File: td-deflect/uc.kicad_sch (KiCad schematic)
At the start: 18 parts, among them J4 Conn_ARM_JTAG_SWD_10, J6 Conn_01x06_Male, U12 LM1117-5.0, U2 STM32G474xx, U3 INA193, U4 TPS70933, X1 SG-8002CA

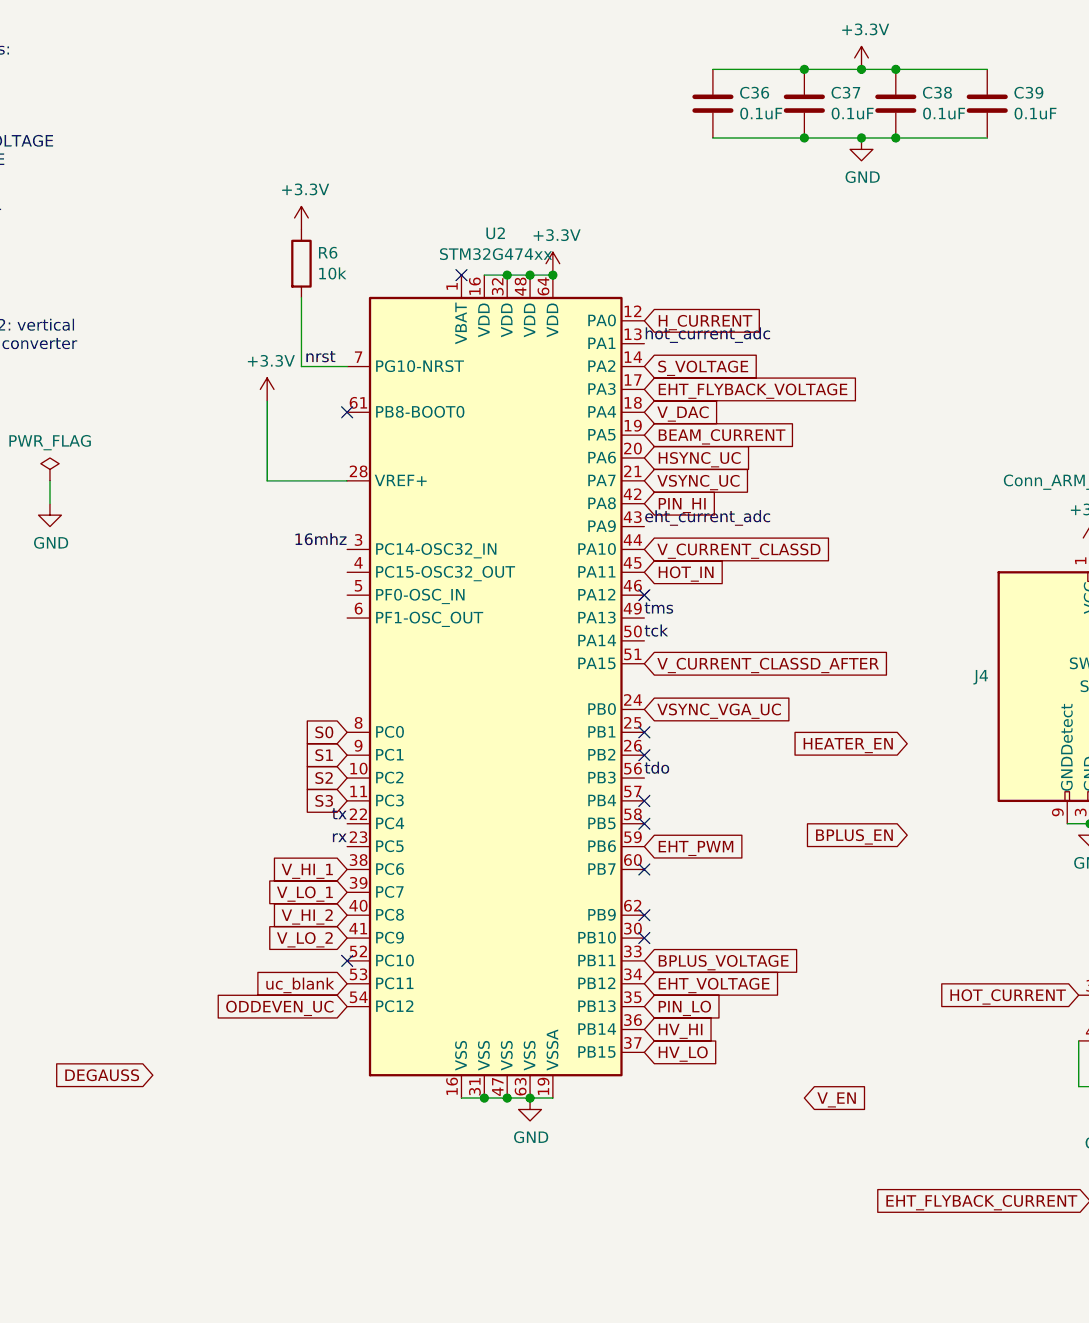
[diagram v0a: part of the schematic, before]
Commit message: switch to kicad official uc symbol
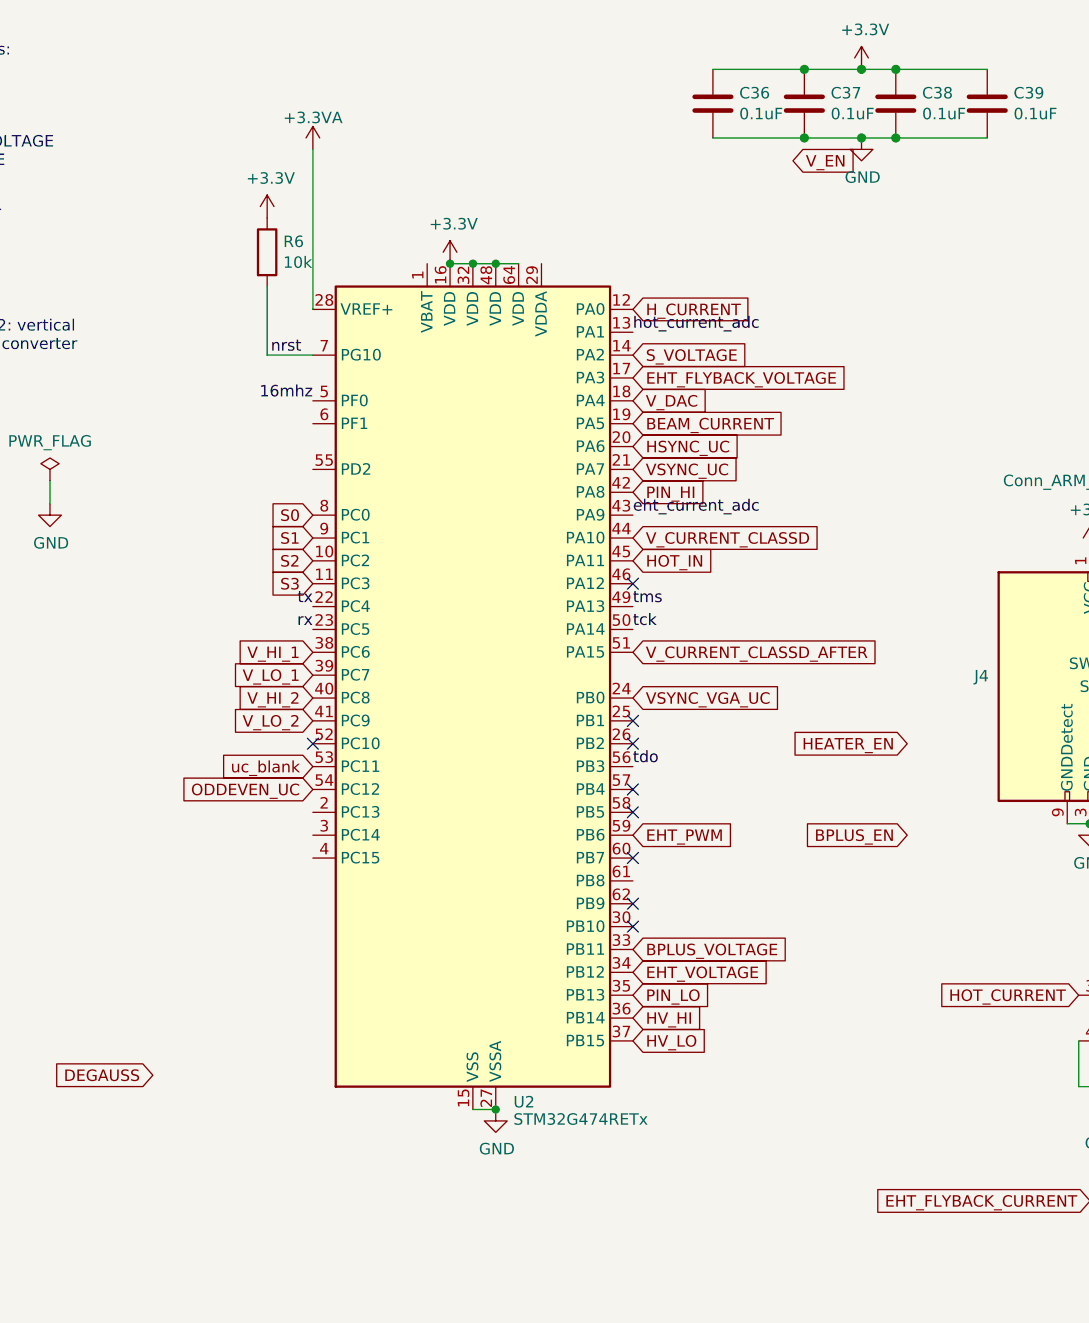
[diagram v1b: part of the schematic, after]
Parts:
- removed U2: STM32G474xx, Package_QFP:LQFP-64_10x10mm_P0.5mm, symbol td-crt:STM32G474xx
- added U2: STM32G474RETx, Package_QFP:LQFP-64_10x10mm_P0.5mm, symbol MCU_ST_STM32G4:STM32G474RETx
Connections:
- net +3V3: now also U2.16 (VDD), U2.32 (VDD), U2.48 (VDD), U2.64 (VDD)
- net 16mhz: now also U2.5 (PF0)
- net BEAM_CURRENT: now also U2.19 (PA5)
- net BPLUS_VOLTAGE: now also U2.33 (PB11)
- net EHT_FLYBACK_VOLTAGE: now also U2.17 (PA3)
- net EHT_PWM: now also U2.59 (PB6)
- net EHT_VOLTAGE: now also U2.34 (PB12)
- net GND: now also U2.15 (VSS), U2.27 (VSSA), U2.31 (VSS), U2.47 (VSS), U2.63 (VSS)
- net HOT_IN: now also U2.45 (PA11)
- net HSYNC_UC: now also U2.20 (PA6)
- net HV_HI: now also U2.36 (PB14)
- net HV_LO: now also U2.37 (PB15)
- net H_CURRENT: now also U2.12 (PA0)
- net ODDEVEN_UC: now also U2.54 (PC12)
- net PIN_HI: now also U2.42 (PA8)
- net PIN_LO: now also U2.35 (PB13)
- net S0: now also U2.8 (PC0)
- net S1: now also U2.9 (PC1)
- net S2: now also U2.10 (PC2)
- net S3: now also U2.11 (PC3)
- net S_VOLTAGE: now also U2.14 (PA2)
- net VSYNC_UC: now also U2.21 (PA7)
- net VSYNC_VGA_UC: now also U2.24 (PB0)
- net V_CURRENT_CLASSD: now also U2.44 (PA10)
- net V_CURRENT_CLASSD_AFTER: now also U2.51 (PA15)
- net V_DAC: now also U2.18 (PA4)
- net V_HI_1: now also U2.38 (PC6)
- net V_HI_2: now also U2.40 (PC8)
- net V_LO_1: now also U2.39 (PC7)
- net V_LO_2: now also U2.41 (PC9)
- net eht_current_adc: now also U2.43 (PA9)
- net hot_current_adc: now also U2.13 (PA1)
- net nrst: now also U2.7 (PG10)
- net rx: now also U2.23 (PC5)
- net tck: now also U2.50 (PA14)
- net tdo: now also U2.56 (PB3)
- net tms: now also U2.49 (PA13)
- net tx: now also U2.22 (PC4)
- net uc_blank: now also U2.53 (PC11)
- new net +3.3VA: U2.28 (VREF+)
- no-connect marks 15 -> 13

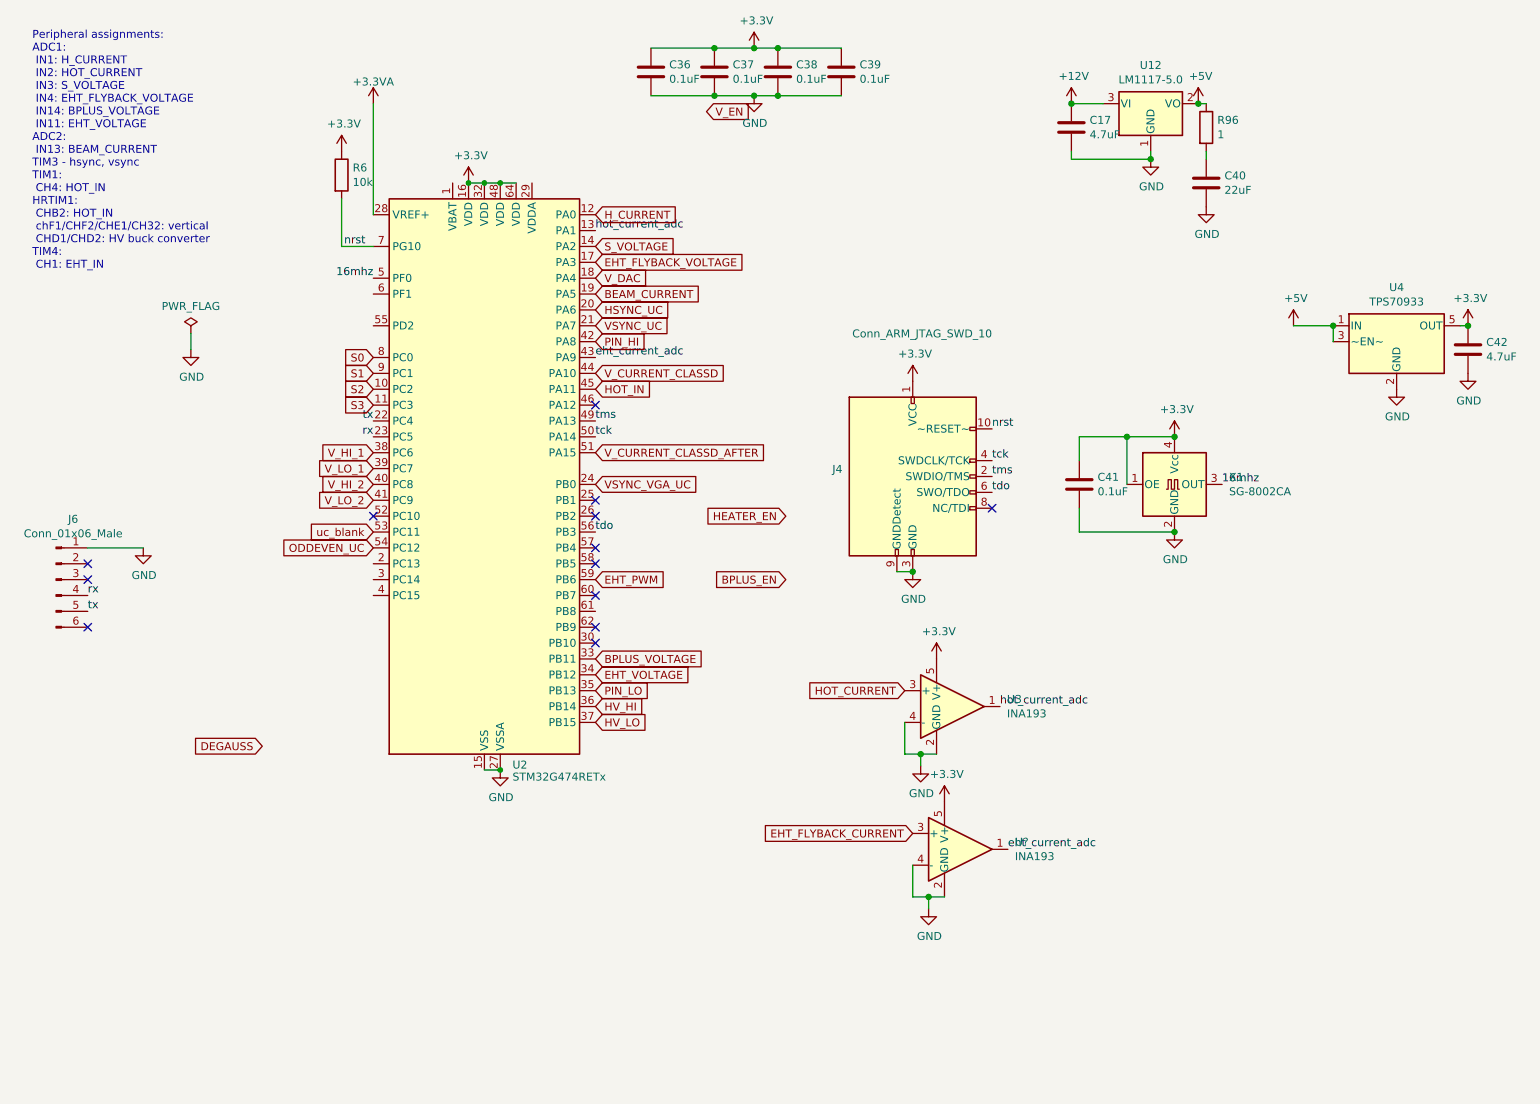
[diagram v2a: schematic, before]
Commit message: add separate analog power supply
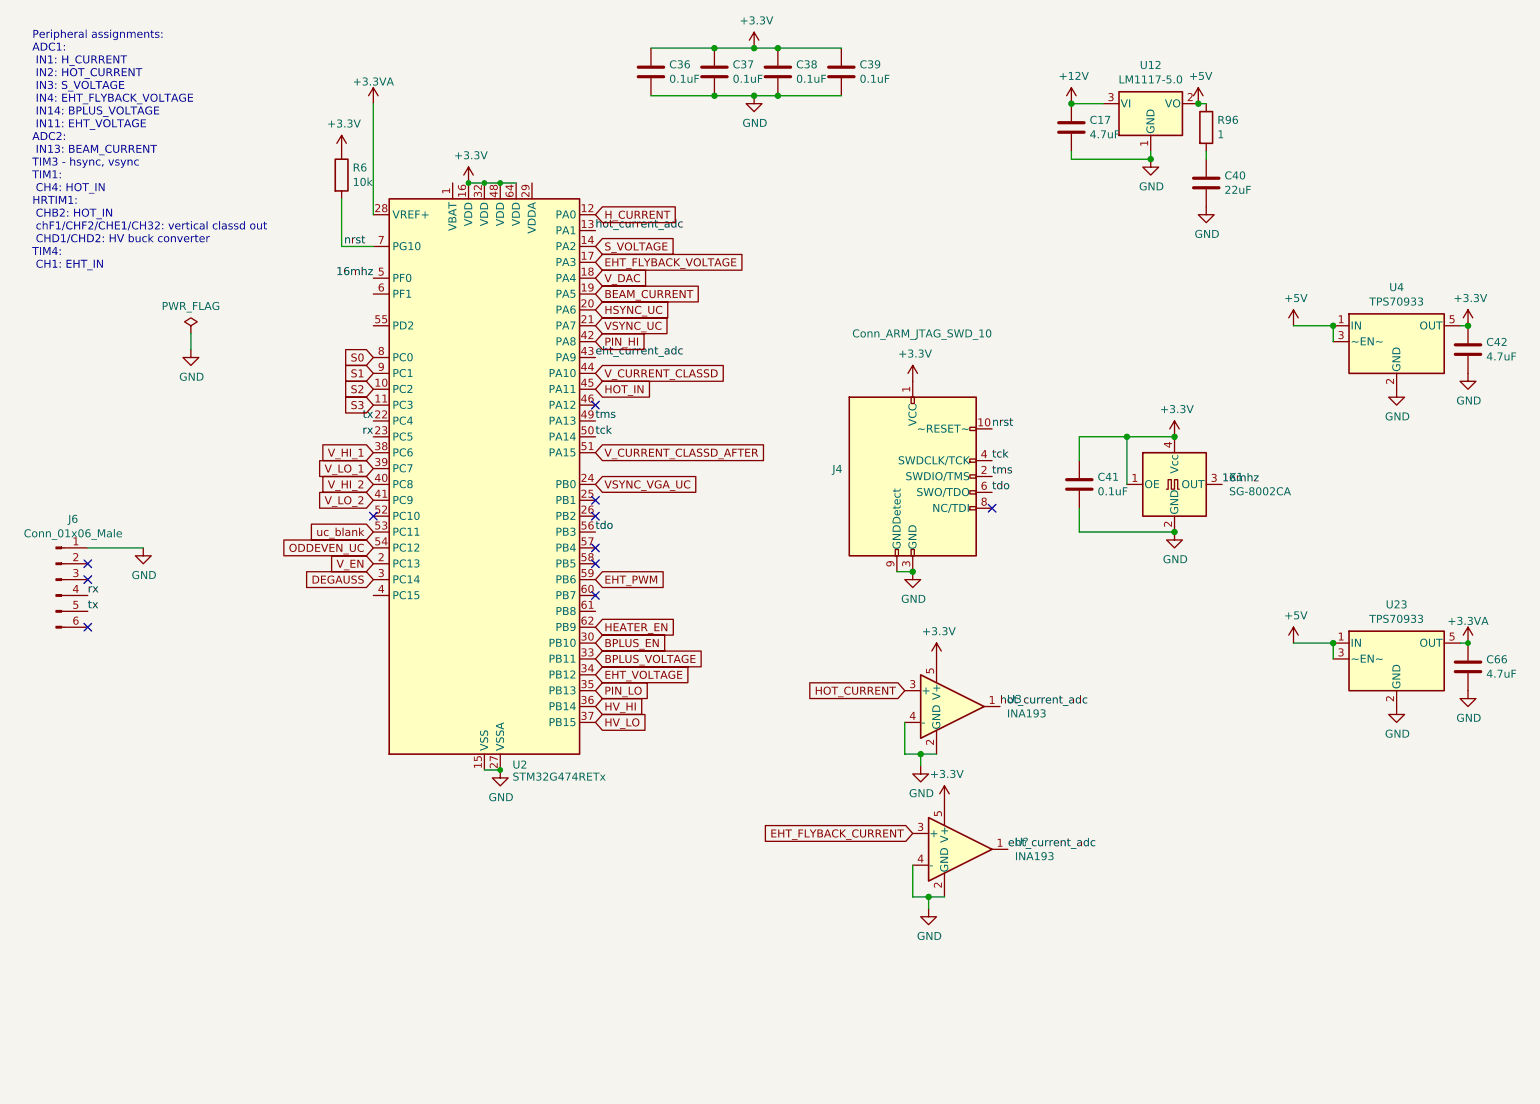
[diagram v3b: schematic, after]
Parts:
- added C66: 4.7uF, Capacitor_SMD:C_0805_2012Metric_Pad1.15x1.40mm_HandSolder, symbol Device:C
- added U23: TPS70933, Package_TO_SOT_SMD:SOT-23-5, symbol td-deflect-rescue:TPS76933-Regulator_Linear
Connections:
- net +3.3VA: now also C66.1, U23.5 (OUT)
- net +5V: now also U23.1 (IN), U23.3 (~EN~)
- net BPLUS_EN: now also U2.30 (PB10)
- net DEGAUSS: now also U2.3 (PC14)
- net GND: now also C66.2, U23.2 (GND)
- net HEATER_EN: now also U2.62 (PB9)
- net V_EN: now also U2.2 (PC13)
- no-connect marks 13 -> 11
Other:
- note added: "Peripheral assignments: ADC1: IN1: H_CURRENT IN2: HOT_CURRENT IN3: S_VOLTAGE IN4: EHT_FLYBACK_VOLTAGE IN14: BPLUS_VOLTAGE IN11: EHT_VOLTAGE ADC2: IN13: BEAM_CURRENT TIM3 - hsync, vsync TIM1: CH4: HOT_IN HRTIM1: CHB2: HOT_IN chF1/CHF2/CHE1/CH32: vertical classd out CHD1/CHD2: HV buck converter TIM4: CH1: EHT_IN"
- note removed: "Peripheral assignments: ADC1: IN1: H_CURRENT IN2: HOT_CURRENT IN3: S_VOLTAGE IN4: EHT_FLYBACK_VOLTAGE IN14: BPLUS_VOLTAGE IN11: EHT_VOLTAGE ADC2: IN13: BEAM_CURRENT TIM3 - hsync, vsync TIM1: CH4: HOT_IN HRTIM1: CHB2: HOT_IN chF1/CHF2/CHE1/CH32: vertical CHD1/CHD2: HV buck converter TIM4: CH1: EHT_IN"
